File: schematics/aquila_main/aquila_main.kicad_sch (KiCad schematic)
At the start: 95 parts, among them IC1 TPS62152, IC2 TPS62132

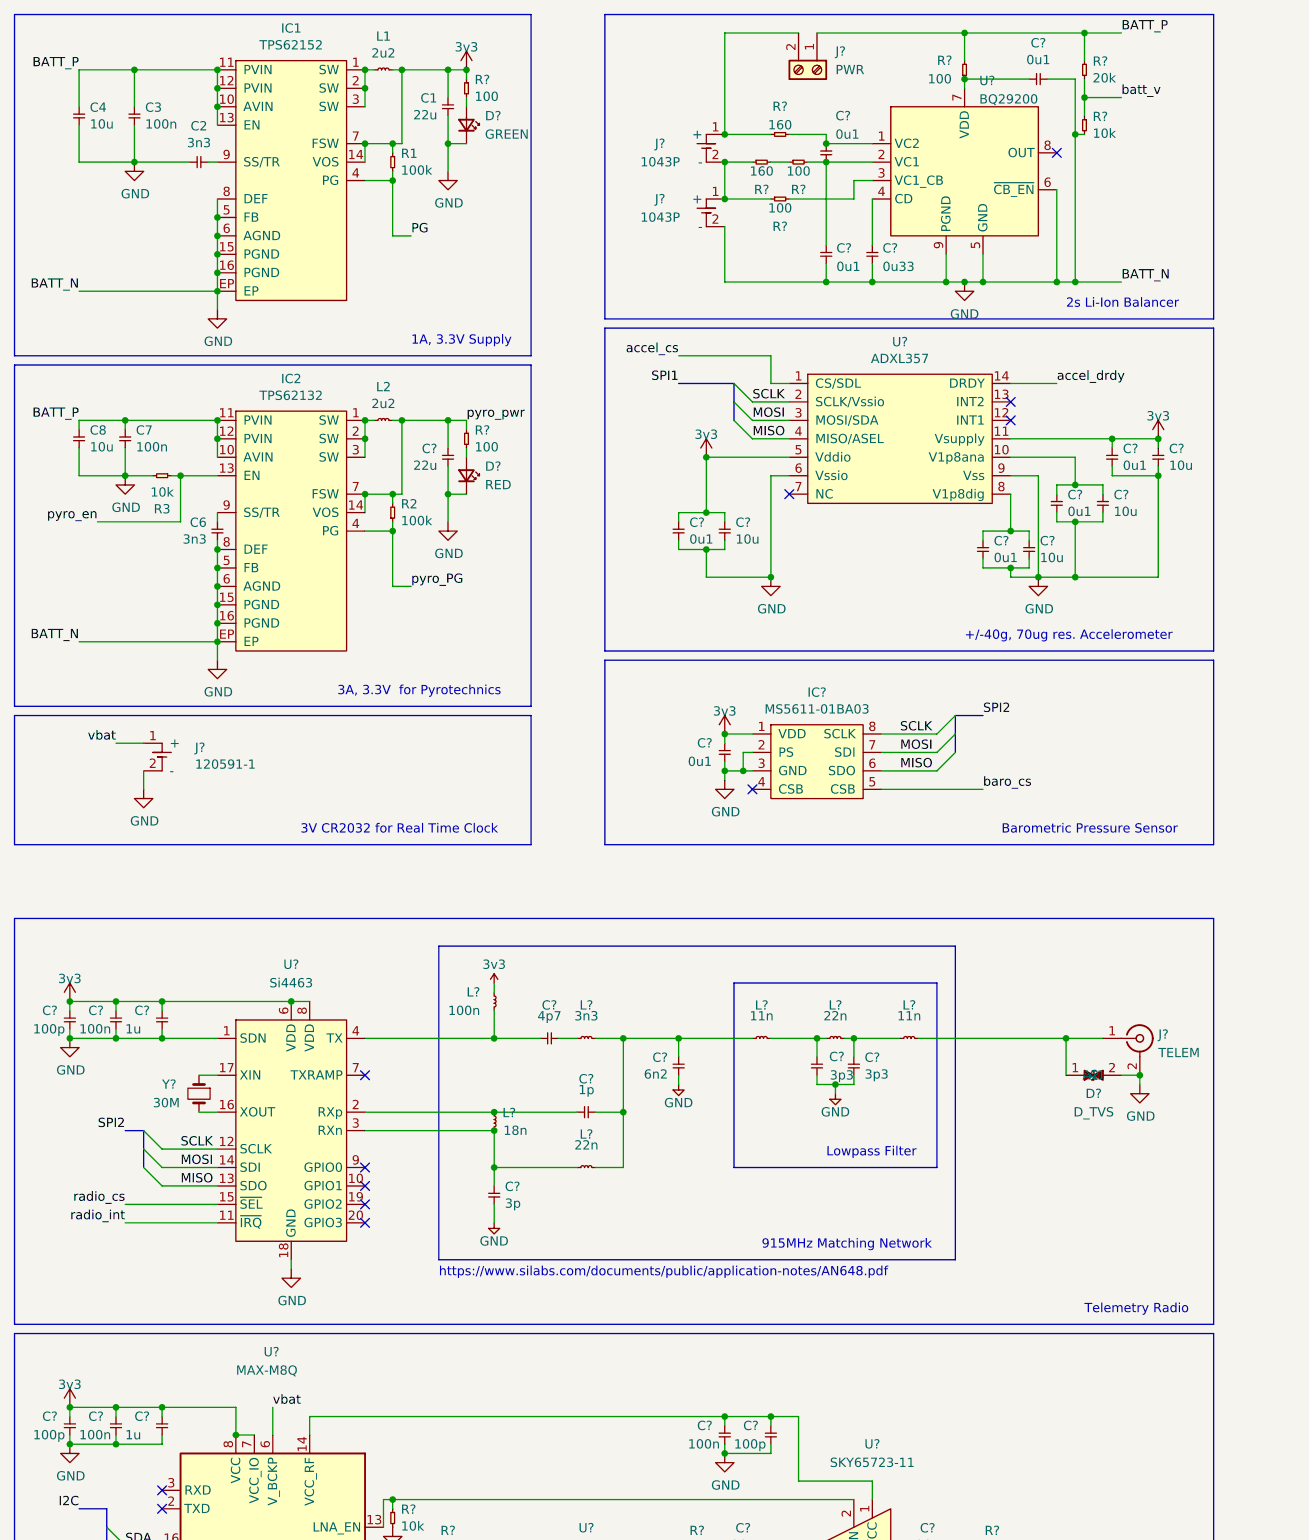
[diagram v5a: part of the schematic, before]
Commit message: fixed net label formatting
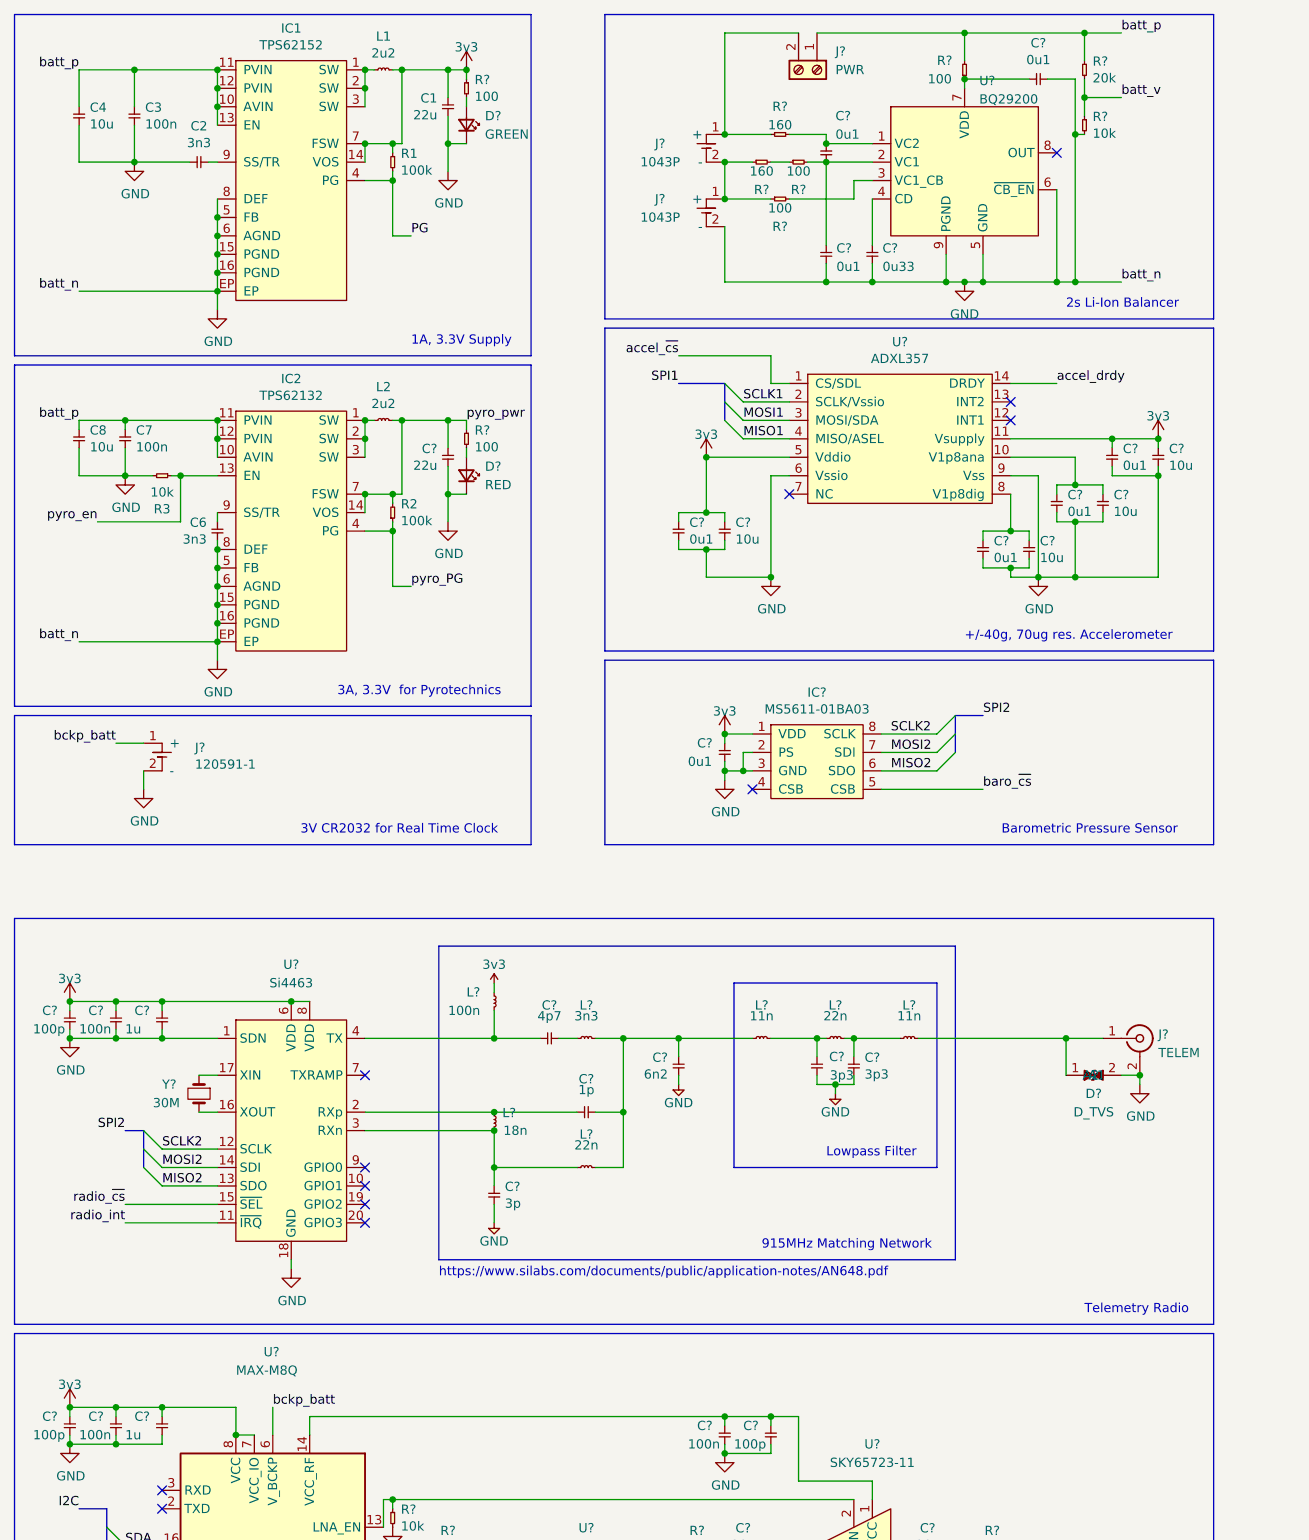
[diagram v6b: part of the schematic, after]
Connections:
- net BATT_P renamed batt_p
- net MISO renamed MISO2
- net MISO2: no longer U?.4 (MISO/ASEL)
- net MOSI renamed MOSI2
- net MOSI2: no longer U?.3 (MOSI/SDA)
- net SCLK renamed SCLK2
- net SCLK2: no longer U?.2 (SCLK/Vssio)
- net accel_cs renamed accel_~{cs}
- net baro_cs renamed baro_~{cs}
- net radio_cs renamed radio_~{cs}
- net vbat renamed bckp_batt
- new net MISO1: U?.4 (MISO/ASEL)
- new net MOSI1: U?.3 (MOSI/SDA)
- new net SCLK1: U?.2 (SCLK/Vssio)
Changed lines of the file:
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@@
     (stroke (width 0) (type default) (color 0 0 0 0))
   )
-  (bus_entry (at 124.46 76.2) (size 2.54 2.54)
-    (stroke (width 0) (type default) (color 0 0 0 0))
-  )
-  (bus_entry (at 124.46 71.12) (size 2.54 2.54)
+  (bus_entry (at 123.19 76.2) (size 2.54 2.54)
+    (stroke (width 0) (type default) (color 0 0 0 0))
+  )
+  (bus_entry (at 123.19 71.12) (size 2.54 2.54)
     (stroke (width 0) (type default) (color 0 0 0 0))
   )
@@
     (stroke (width 0) (type default) (color 0 0 0 0))
   )
-  (bus_entry (at 124.46 73.66) (size 2.54 2.54)
+  (bus_entry (at 123.19 73.66) (size 2.54 2.54)
     (stroke (width 0) (type default) (color 0 0 0 0))
   )
@@
     (stroke (width 0) (type default) (color 0 0 0 0))
   )
-  (bus (pts (xy 124.46 71.12) (xy 124.46 73.66))
+  (bus (pts (xy 123.19 71.12) (xy 123.19 73.66))
     (stroke (width 0) (type default) (color 0 0 0 0))
   )
@@
     (stroke (width 0) (type default) (color 0 0 0 0))
   )
-  (wire (pts (xy 132.08 76.2) (xy 127 76.2))
+  (wire (pts (xy 132.08 76.2) (xy 125.73 76.2))
     (stroke (width 0) (type default) (color 0 0 0 0))
   )
@@
     (stroke (width 0) (type default) (color 0 0 0 0))
   )
-  (wire (pts (xy 132.08 73.66) (xy 127 73.66))
+  (wire (pts (xy 132.08 73.66) (xy 125.73 73.66))
     (stroke (width 0) (type default) (color 0 0 0 0))
   )
@@
     (stroke (width 0) (type default) (color 0 0 0 0))
   )
-  (bus (pts (xy 124.46 71.12) (xy 116.84 71.12))
+  (bus (pts (xy 123.19 71.12) (xy 116.84 71.12))
     (stroke (width 0) (type default) (color 0 0 0 0))
   )
@@
     (stroke (width 0) (type default) (color 0 0 0 0))
   )
-  (bus (pts (xy 124.46 73.66) (xy 124.46 76.2))
+  (bus (pts (xy 123.19 73.66) (xy 123.19 76.2))
     (stroke (width 0) (type default) (color 0 0 0 0))
   )
@@
     (stroke (width 0) (type default) (color 0 0 0 0))
   )
-  (wire (pts (xy 127 78.74) (xy 132.08 78.74))
+  (wire (pts (xy 125.73 78.74) (xy 132.08 78.74))
     (stroke (width 0) (type default) (color 0 0 0 0))
   )
@@
     (effects (font (size 1.27 1.27)) (justify left bottom))
   )
-  (label "MOSI" (at 48.26 179.07 0)
-    (effects (font (size 1.27 1.27)) (justify left bottom))
-  )
-  (label "BATT_P" (at 34.29 27.94 180)
+  (label "MOSI2" (at 45.72 179.07 0)
+    (effects (font (size 1.27 1.27)) (justify left bottom))
+  )
+  (label "batt_p" (at 34.29 27.94 180)
     (effects (font (size 1.27 1.27)) (justify right bottom))
   )
@@
     (effects (font (size 1.27 1.27)) (justify left bottom))
   )
-  (label "BATT_P" (at 177.8 22.86 0)
-    (effects (font (size 1.27 1.27)) (justify left bottom))
-  )
-  (label "vbat" (at 60.96 212.09 0)
+  (label "batt_p" (at 177.8 22.86 0)
+    (effects (font (size 1.27 1.27)) (justify left bottom))
+  )
+  (label "bckp_batt" (at 60.96 212.09 0)
     (effects (font (size 1.27 1.27)) (justify left bottom))
   )
@@
     (effects (font (size 1.27 1.27)) (justify right bottom))
   )
-  (label "MOSI" (at 147.32 121.92 0)
-    (effects (font (size 1.27 1.27)) (justify left bottom))
-  )
-  (label "SCLK" (at 127 73.66 0)
+  (label "MOSI2" (at 146.05 121.92 0)
+    (effects (font (size 1.27 1.27)) (justify left bottom))
+  )
+  (label "SCLK1" (at 125.73 73.66 0)
     (effects (font (size 1.27 1.27)) (justify left bottom))
   )
@@
     (effects (font (size 1.27 1.27)) (justify left bottom))
   )
-  (label "accel_cs" (at 116.84 67.31 180)
+  (label "accel_~{cs}" (at 116.84 67.31 180)
     (effects (font (size 1.27 1.27)) (justify right bottom))
   )
@@
     (effects (font (size 1.27 1.27)) (justify right bottom))
   )
-  (label "MISO" (at 147.32 124.46 0)
+  (label "MISO2" (at 146.05 124.46 0)
     (effects (font (size 1.27 1.27)) (justify left bottom))
   )
@@
     (effects (font (size 1.27 1.27)) (justify left bottom))
   )
-  (label "SCLK" (at 48.26 176.53 0)
+  (label "SCLK2" (at 45.72 176.53 0)
     (effects (font (size 1.27 1.27)) (justify left bottom))
   )
@@
     (effects (font (size 1.27 1.27)) (justify right bottom))
   )
-  (label "radio_cs" (at 40.64 184.15 180)
+  (label "radio_~{cs}" (at 40.64 184.15 180)
     (effects (font (size 1.27 1.27)) (justify right bottom))
   )
-  (label "BATT_N" (at 34.29 58.42 180)
+  (label "batt_n" (at 34.29 58.42 180)
     (effects (font (size 1.27 1.27)) (justify right bottom))
   )
@@
     (effects (font (size 1.27 1.27)) (justify right bottom))
   )
-  (label "BATT_P" (at 34.29 76.2 180)
+  (label "batt_p" (at 34.29 76.2 180)
     (effects (font (size 1.27 1.27)) (justify right bottom))
   )
@@
     (effects (font (size 1.27 1.27)) (justify right bottom))
   )
-  (label "baro_cs" (at 158.75 127 0)
-    (effects (font (size 1.27 1.27)) (justify left bottom))
-  )
-  (label "BATT_N" (at 177.8 57.15 0)
+  (label "baro_~{cs}" (at 158.75 127 0)
+    (effects (font (size 1.27 1.27)) (justify left bottom))
+  )
+  (label "batt_n" (at 177.8 57.15 0)
     (effects (font (size 1.27 1.27)) (justify left bottom))
   )
@@
     (effects (font (size 1.27 1.27)) (justify right bottom))
   )
-  (label "vbat" (at 39.37 120.65 180)
+  (label "bckp_batt" (at 39.37 120.65 180)
     (effects (font (size 1.27 1.27)) (justify right bottom))
   )
-  (label "MOSI" (at 127 76.2 0)
-    (effects (font (size 1.27 1.27)) (justify left bottom))
-  )
-  (label "MISO" (at 48.26 181.61 0)
+  (label "MOSI1" (at 125.73 76.2 0)
+    (effects (font (size 1.27 1.27)) (justify left bottom))
+  )
+  (label "MISO2" (at 45.72 181.61 0)
     (effects (font (size 1.27 1.27)) (justify left bottom))
   )
@@
     (effects (font (size 1.27 1.27)) (justify right bottom))
   )
-  (label "MISO" (at 127 78.74 0)
-    (effects (font (size 1.27 1.27)) (justify left bottom))
-  )
-  (label "BATT_N" (at 34.29 106.68 180)
+  (label "MISO1" (at 125.73 78.74 0)
+    (effects (font (size 1.27 1.27)) (justify left bottom))
+  )
+  (label "batt_n" (at 34.29 106.68 180)
     (effects (font (size 1.27 1.27)) (justify right bottom))
   )
@@
     (effects (font (size 1.27 1.27)) (justify left bottom))
   )
-  (label "SCLK" (at 147.32 119.38 0)
-    (effects (font (size 1.27 1.27)) (justify left bottom))
-  )
+  (label "SCLK2" (at 146.05 119.38 0)
+    (effects (font (size 1.27 1.27)) (justify left bottom))
+  )
